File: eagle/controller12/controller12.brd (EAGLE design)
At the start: 30 x 65 mm, 60 parts, among them IC1 ILD213T, J2 AVR_SPI_PRG_62X3_LOCK, Q2 200mA/50V, Q4 200mA/50V, Q5 200mA/50V, U3 MP2307, X1 1501_04, X2 ZX62D-B-5PA8

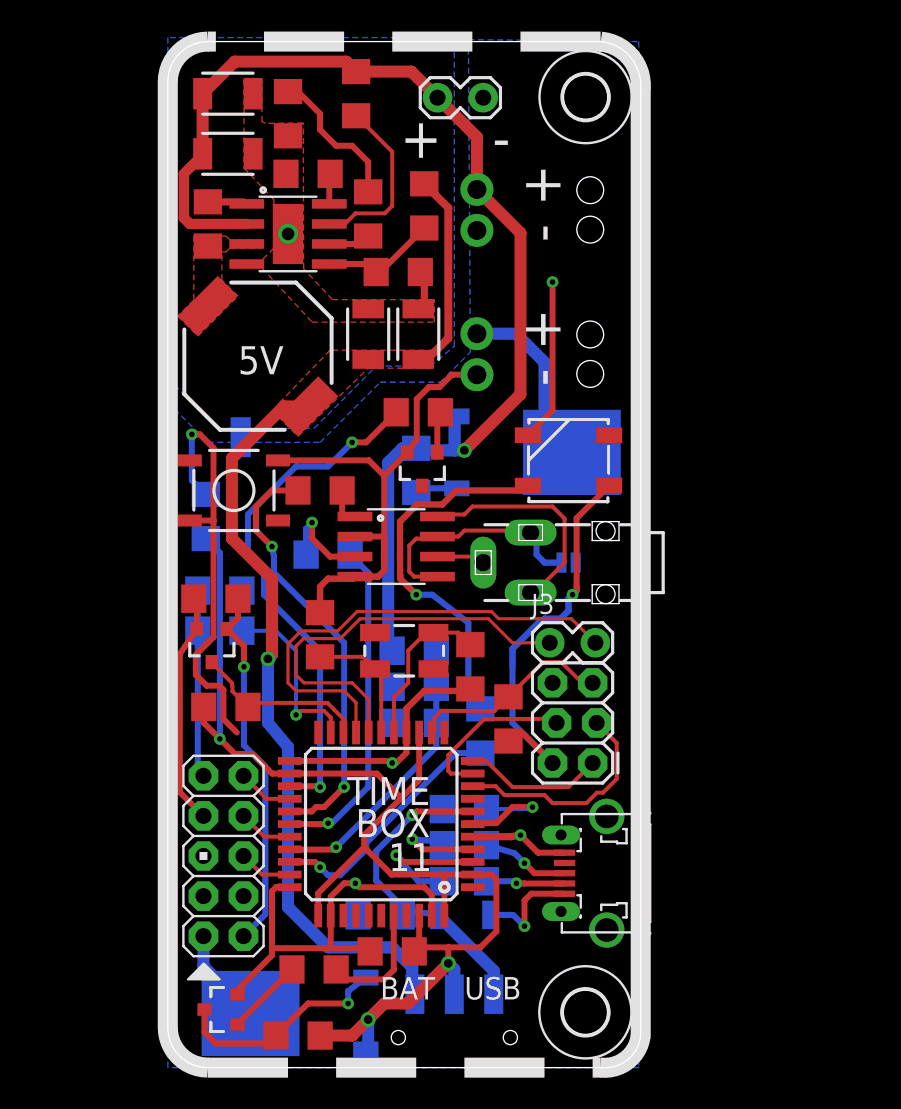
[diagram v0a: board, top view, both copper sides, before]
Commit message: controller12: added header for possible extension board
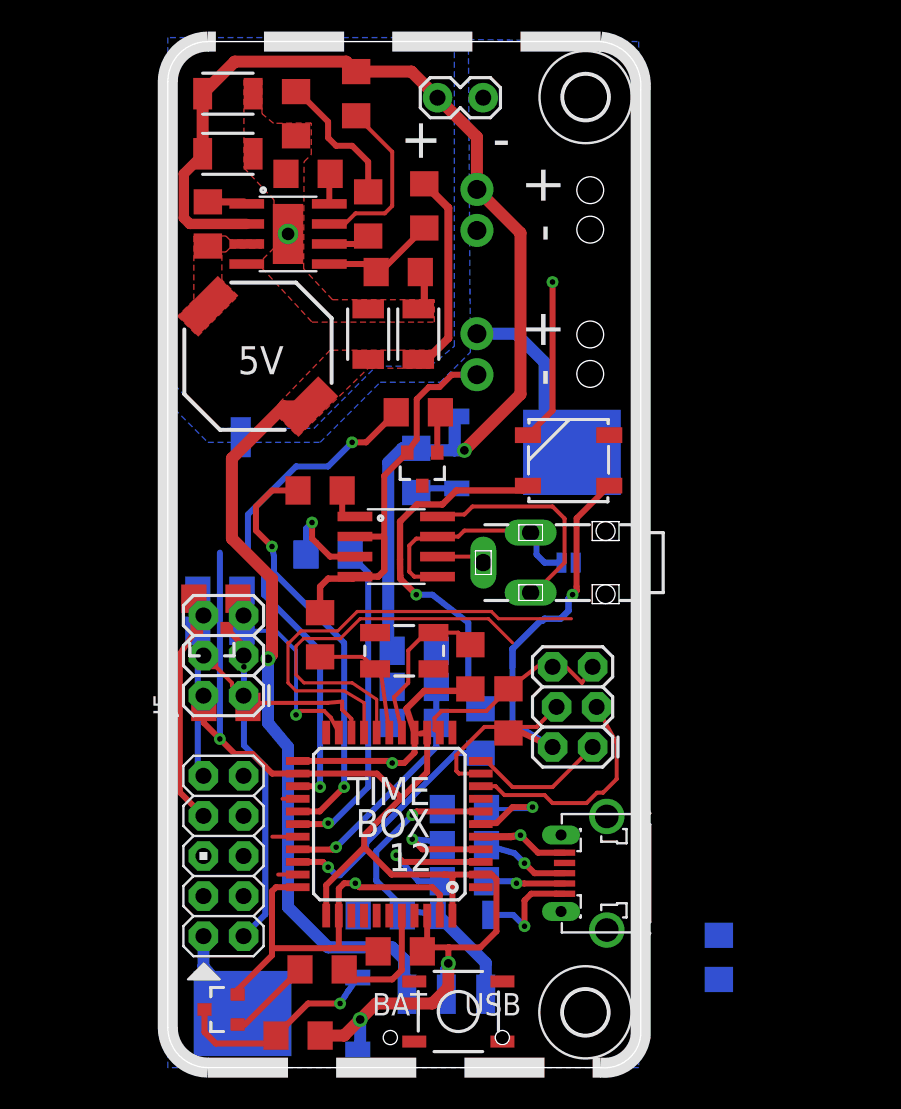
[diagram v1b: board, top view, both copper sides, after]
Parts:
- removed J3: (no value), SparkFun-Connectors:1X02_LOCK
- added J5: FEMALE 2x3, SparkFun-Connectors:2X3
- moved R5 42.9 mm to (34.9, 6.99)
- moved S1 36.0 mm to (18.4, 3.56)
- moved J2 1.02 mm to (26.9, 20.3)
- moved RRST 0.51 mm to (21.6, 22.6)
- moved S2 0.51 mm to (17.7, 1.91)
- moved Q3 0.51 mm to (7.24, 3.43)
- moved R1 0.51 mm to (8.13, 60.5)
- moved C1 0.51 mm to (14.7, 7.37)
- moved R6 0.51 mm to (9.78, 6.22)
- moved U$3 0.51 mm to (14.0, 15.4)
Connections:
- net SCL: no longer J3.1
- net SDA: no longer J3.2
- net Z_GPIO_1: no longer J1.2
- net Z_GPIO_2: no longer J1.4
- net Z_GPIO_3: no longer J1.6
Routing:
- net BTN: track 28.4 -> 0.00 mm, vias 1 -> 0
- net GND: track 89.9 -> 84.1 mm
- net Z_GPIO_1: track 3.53 -> 0.97 mm
- net Z_GPIO_3: track 3.42 -> 1.25 mm
- net VCC: track 107.9 -> 105.9 mm
- net SCL: track 26.6 -> 24.6 mm
- net Z_GPIO_2: track 3.47 -> 1.61 mm
- net SDA: track 30.4 -> 28.6 mm
- net RX: track 11.2 -> 12.1 mm
- net N$3: track 14.1 -> 13.4 mm
- net RST: track 13.0 -> 13.6 mm
- net N$2: track 4.92 -> 5.44 mm
- net N$5: track 6.07 -> 6.58 mm
- net N$4: track 8.71 -> 9.22 mm
- net LED: track 15.9 -> 15.4 mm
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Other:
- board text added: "12"
- board text removed: "11"

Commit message: controller12 routing improved
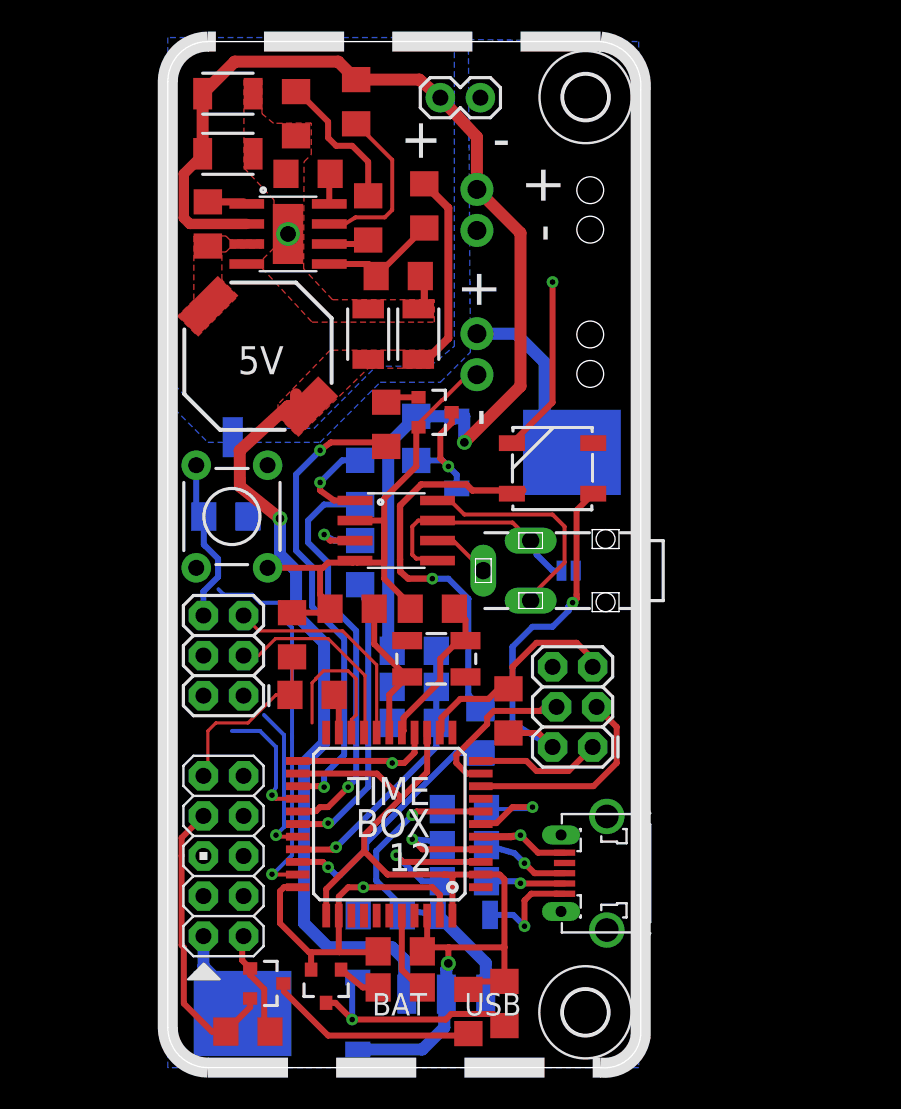
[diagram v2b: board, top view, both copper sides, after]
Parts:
- J4: device SparkFun-Connectors:1X02_LOCK -> SparkFun-Connectors:1X02
- S1: device SparkFun-Retired:TACTILE-SWITCH-SMD -> SparkFun-Retired:TACTILE-PTH
- moved R5 41.9 mm to (3.68, 34.9), turned to 0 degrees
- moved S1 34.5 mm to (4.06, 34.9), turned to 270 degrees
- moved R7 27.5 mm to (5.08, 2.29)
- moved R8 24.7 mm to (19.1, 3.56), turned to 270 degrees
- moved Q5 21.7 mm to (6.22, 5.33), turned to 270 degrees
- moved R4 13.2 mm to (21.3, 4.06), turned to 270 degrees
- moved R11 7.12 mm to (9.14, 23.6), flipped to the top, turned to 180 degrees
- moved Q4 6.78 mm to (10.0, 5.21), turned to 180 degrees
- moved R12 5.36 mm to (7.87, 27.4), flipped to the top, turned to 90 degrees
- moved R6 5.08 mm to (14.7, 5.08)
- moved C5 4.40 mm to (16.8, 29.1), turned to 0 degrees
- moved Q2 3.64 mm to (16.9, 41.5), turned to 270 degrees
- moved C4 2.62 mm to (11.7, 29.1), turned to 0 degrees
- moved R20 2.59 mm to (12.2, 37.1), flipped to the bottom, turned to 90 degrees
- moved R10 2.17 mm to (13.8, 40.8), turned to 90 degrees
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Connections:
- net Z_GPIO_1 renamed EXT_3
- removed net Z_GPIO_2: U$3.29
- removed net Z_GPIO_3: U$3.32
- new net EXT_1: J5.1, U$3.32
- new net EXT_2: J5.2, U$3.29
- net BTN: now also J5.6
- net SCL: now also J5.5
- net SDA: now also J5.3
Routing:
- net EXT_1: track 0.00 -> 24.6 mm, vias 0 -> 1
- net VCC: track 105.9 -> 86.2 mm, vias 4 -> 2
- net ZERO_3.3V: track 23.3 -> 6.81 mm, vias 1 -> 0
- net SDA: track 28.6 -> 12.7 mm
- net RX: track 12.1 -> 22.8 mm
- net SCL: track 24.6 -> 14.0 mm
- net BTN: track 0.00 -> 10.5 mm
- net EXT_2: track 0.00 -> 9.78 mm, vias 0 -> 1
- net TX: track 11.6 -> 2.46 mm, vias 1 -> 0
- net EXT_3: track 0.97 -> 8.05 mm, vias 0 -> 1
- net N$1: track 3.47 -> 7.74 mm, vias 0 -> 1
- net ZERO_TX: track 14.8 -> 18.7 mm
- net N$19: track 2.46 -> 6.04 mm, vias 0 -> 1
- net CAM_EN: track 32.7 -> 29.9 mm
- net N$2: track 5.44 -> 2.75 mm
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
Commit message: controller 12 progress zero_standalone enclosure
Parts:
- added D1: MBRS130LT3, diode:SMB
- J2: value AVR_SPI_PRG_62X3_LOCK -> AVR_SPI_PRG_6PTH; device SparkFun-Connectors:2X3_LOCK -> SparkFun-Connectors:2X3
- moved C14 5.34 mm to (12.4, 59.2), turned to 0 degrees
- moved R2 1.02 mm to (14.6, 51.2)
- moved R24 0.72 mm to (12.4, 61.7), turned to 0 degrees
- moved R3 0.72 mm to (16.8, 55.1), turned to 270 degrees
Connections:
- removed net EXT_3: U$3.26
- new net FOO5: U$3.36
- net BTN: now also J5.4, S1.4, U$3.26; no longer J5.6, S1.3, U$3.36
- net GND: now also J5.6
- net GNDA: now also D1.A
- net N$26: now also D1.C
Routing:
- net VCC: track 86.2 -> 106.6 mm, vias 2 -> 3
- net RX: track 22.8 -> 42.4 mm
- net BTN: track 10.5 -> 26.1 mm, vias 0 -> 1
- net EXT_1: track 24.6 -> 15.5 mm
- net EXT_3: track 8.05 -> 0.00 mm, vias 1 -> 0
- net N$29: track 2.52 -> 9.21 mm
- net N$28: track 9.17 -> 4.02 mm
- net EXT_2: track 9.78 -> 13.8 mm
- net CONV_5V: track 62.7 -> 59.4 mm
- net BATT_VCC: track 76.2 -> 78.6 mm
- net N$30: track 8.01 -> 9.89 mm
- net ZERO_RX: track 11.6 -> 10.3 mm
- net GNDA: track 2.64 -> 3.28 mm
- net N$9: track 10.1 -> 10.7 mm

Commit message: controller12: sidebar
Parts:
- moved R5 38.6 mm to (42.3, 36.4)
- moved S1 34.0 mm to (35.6, 22.2)
- moved J2 25.9 mm to (4.80, 33.7)
- moved RRST 20.4 mm to (40.9, 29.2)
- moved R11 14.8 mm to (-5.59, 24.6)
- moved R12 14.2 mm to (-5.08, 21.6), turned to 0 degrees
- moved C4 11.8 mm to (22.7, 24.9), turned to 90 degrees
- moved C5 5.82 mm to (20.2, 24.4), turned to 90 degrees
- moved Y1 0.80 mm to (16.8, 25.1), turned to 90 degrees
- moved C13 0.51 mm to (2.54, 54.0)
- moved C16 0.51 mm to (15.9, 47.0)
- moved C17 0.51 mm to (12.7, 47.0)
- moved C19 0.51 mm to (3.81, 58.4)
- moved L2 0.51 mm to (5.71, 45.6)
- moved U3 0.51 mm to (7.62, 53.3)
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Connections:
- net GND: no longer J5.6
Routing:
- net MOSI: track 9.94 -> 44.1 mm
- net RX: track 42.4 -> 13.4 mm
- net SCK: track 13.5 -> 39.1 mm
- net GND: track 82.5 -> 66.5 mm
- net VCC: track 106.6 -> 91.1 mm, vias 3 -> 2
- net N$9: track 10.7 -> 0.00 mm
- net BTN: track 26.1 -> 15.6 mm
- net ZERO_RX: track 10.3 -> 0.00 mm
- net N$8: track 9.18 -> 0.00 mm
- net RST: track 14.1 -> 6.67 mm
- net CONV_5V: track 59.4 -> 56.3 mm
- net MISO: track 7.98 -> 10.7 mm
- net N$27: track 2.52 -> 3.49 mm
- net PB_BUCK_EN: track 10.5 -> 11.3 mm
- net EXT_1: track 15.5 -> 14.8 mm
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
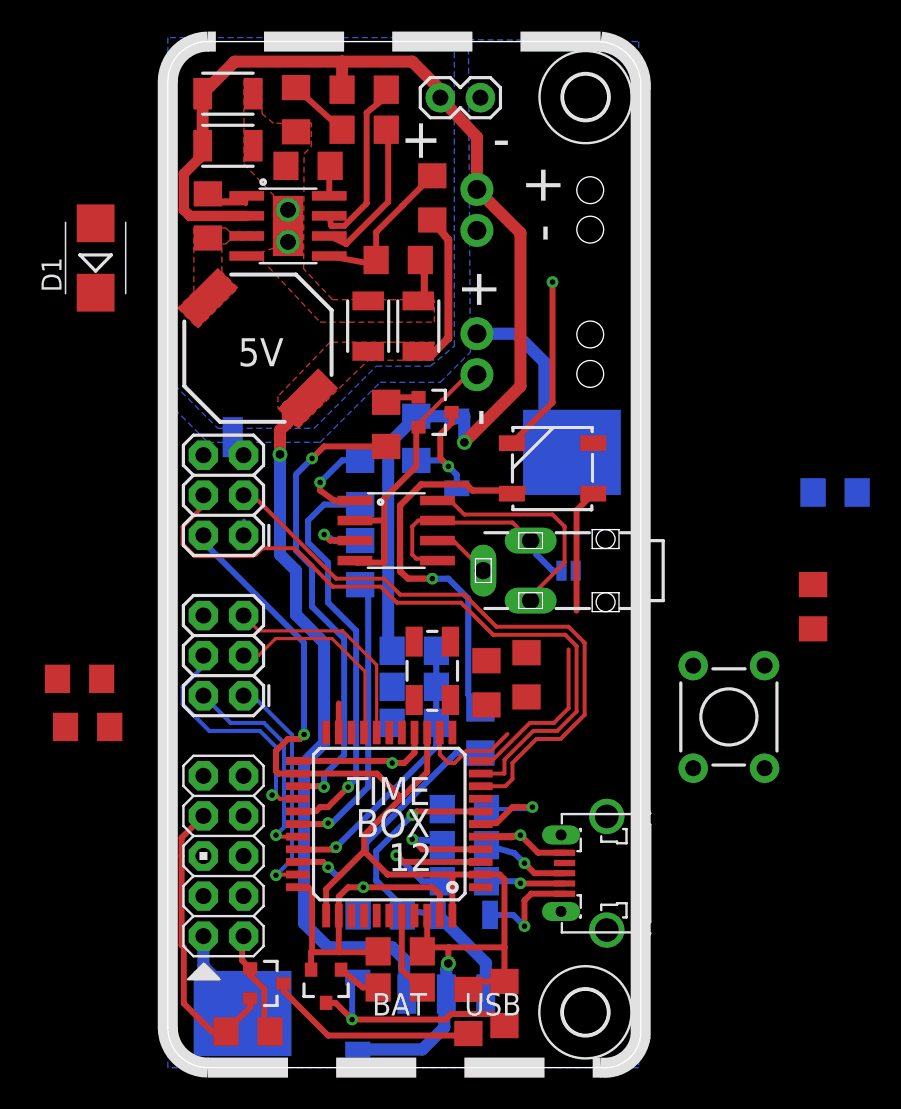
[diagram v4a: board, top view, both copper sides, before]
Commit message: controller12: added 5k resistor to allow to use AREF either with a voltage divider, without one or not at all
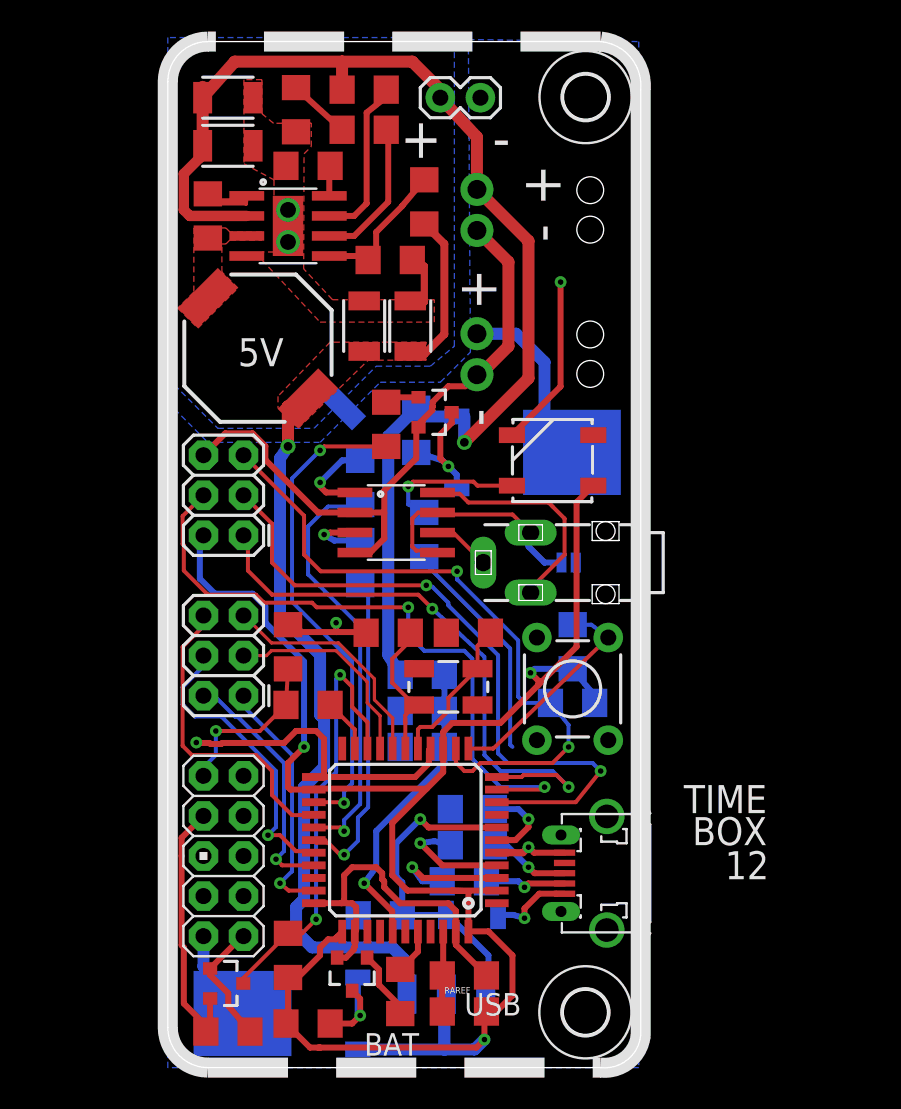
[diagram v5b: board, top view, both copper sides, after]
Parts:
- removed D1: MBRS130LT3, diode:SMB
- added RAREF: 5k, SparkFun-Passives:1206
- moved R5 19.3 mm to (25.7, 26.7), turned to 90 degrees
- moved RRST 16.4 mm to (25.7, 23.1), flipped to the bottom, turned to 180 degrees
- moved R11 14.6 mm to (8.89, 23.0)
- moved R12 13.7 mm to (7.62, 26.7), turned to 90 degrees
- moved R_LED 12.9 mm to (16.3, 33.8)
- moved R4 12.5 mm to (8.89, 2.79), turned to 0 degrees
- moved R8 12.0 mm to (7.62, 7.11), turned to 90 degrees
- moved S1 10.1 mm to (25.7, 24.0), turned to 90 degrees
- moved C4 9.16 mm to (14.0, 27.6), turned to 0 degrees
- moved SH2 7.33 mm to (11.2, 41.7), turned to 45 degrees
- moved C1 4.34 mm to (18.8, 5.84), turned to 180 degrees
- moved C5 3.37 mm to (19.1, 27.6), turned to 0 degrees
- moved Q5 2.54 mm to (3.68, 5.33)
- moved Q4 1.82 mm to (11.7, 5.97)
- moved C6 1.61 mm to (16.1, 20.3)
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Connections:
- net EXT_1 renamed EXT1
- removed net EXT_2: J5.2, U$3.29
- removed net FOO1: U$3.38
- removed net VD_DIRECT: C6.1, U$3.30, VD1.1, VD2.2
- new net EXT2: J5.2, U$3.30
- new net EXT3: J5.4, U$3.29
- new net EXT4: J5.6, U$3.26
- new net N$18: C1.2, RAREF.1, U$3.42
- new net VD_INT: C6.1, U$3.38, VD1.1, VD2.2
- net BTN: now also U$3.12; no longer J5.4, U$3.26
- net GNDA: no longer D1.A
- net N$26: no longer D1.C
- net VCC: now also RAREF.2; no longer C1.2, U$3.42
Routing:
- net GND: track 66.5 -> 106.3 mm
- net RST: track 6.67 -> 41.9 mm, vias 0 -> 2
- net VCC: track 91.1 -> 122.1 mm, vias 2 -> 3
- net MISO: track 10.7 -> 37.0 mm, vias 0 -> 2
- net EXT4: track 0.00 -> 19.2 mm
- net VD_INT: track 0.00 -> 19.1 mm, vias 0 -> 1
- net EXT3: track 0.00 -> 18.9 mm, vias 0 -> 1
- net VD_DIRECT: track 18.7 -> 0.00 mm, vias 1 -> 0
- net N$7: track 25.7 -> 9.43 mm
- net EXT2: track 0.00 -> 15.1 mm, vias 0 -> 1
- net RX: track 13.4 -> 28.0 mm, vias 0 -> 2
- net EXT_2: track 13.8 -> 0.00 mm, vias 1 -> 0
- net ZERO_RX: track 0.00 -> 10.6 mm, vias 0 -> 1
- net N$9: track 0.00 -> 9.69 mm
- net N$8: track 0.00 -> 9.39 mm
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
